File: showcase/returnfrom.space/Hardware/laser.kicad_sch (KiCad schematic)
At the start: 12 parts, among them J20 Conn_01x08_Socket, Q2 NPN, U7 LIS2DH

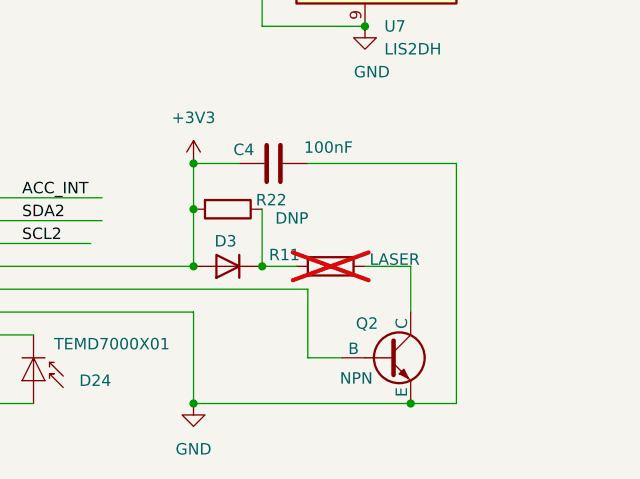
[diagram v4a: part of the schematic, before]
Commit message: Done. Ordered 50pcs. TO DO: clean-up, add BOM & POS
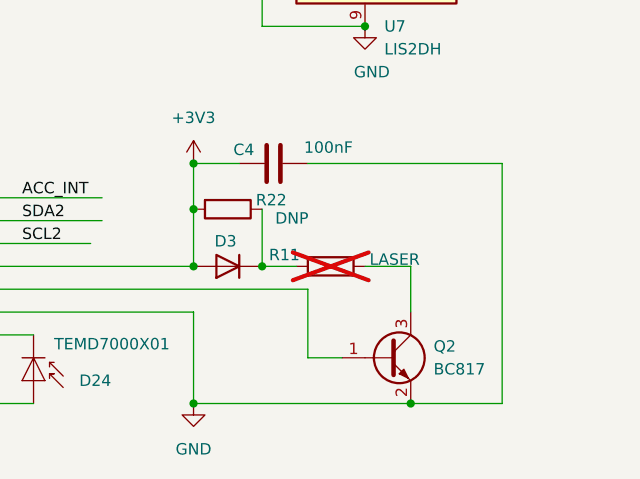
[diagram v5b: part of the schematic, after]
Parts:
- removed Q2: NPN, Package_TO_SOT_SMD:SOT-23, symbol Simulation_SPICE:NPN
- added Q2: BC817, Package_TO_SOT_SMD:SOT-23, symbol Transistor_BJT:BC817
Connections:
- net GND: now also Q2.2 (E)
- net at J20.4 (Pin_4): now also Q2.1 (B)
- net at R11.1: now also Q2.3 (C)
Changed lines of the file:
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@@
 	(paper "A4")
+	(junction
+		(at 204.47 120.65)
+		(diameter 0)
+		(color 0 0 0 0)
+	)
 	(junction
 		(at 180.34 99.06)
@@
 	)
 	(junction
-		(at 204.47 120.65)
-		(diameter 0)
-		(color 0 0 0 0)
-	)
-	(junction
 		(at 187.96 105.41)
 		(diameter 0)
@@
 	(wire
 		(pts
-			(xy 209.55 93.98) (xy 209.55 120.65)
+			(xy 214.63 93.98) (xy 214.63 120.65)
 		)
 		(stroke
@@
 	(wire
 		(pts
-			(xy 193.04 93.98) (xy 209.55 93.98)
+			(xy 193.04 93.98) (xy 214.63 93.98)
 		)
 		(stroke
@@
 	(wire
 		(pts
+			(xy 204.47 120.65) (xy 214.63 120.65)
+		)
+		(stroke
+			(width 0)
+			(type default)
+		)
+	)
+	(wire
+		(pts
 			(xy 158.75 97.79) (xy 170.18 97.79)
 		)
@@
 		(pts
 			(xy 201.93 50.8) (xy 212.09 50.8)
-		)
-		(stroke
-			(width 0)
-			(type default)
-		)
-	)
-	(wire
-		(pts
-			(xy 209.55 120.65) (xy 204.47 120.65)
 		)
 		(stroke
@@
 			)
 			(justify left bottom)
+		)
+	)
+	(symbol
+		(lib_id "Transistor_BJT:BC817")
+		(at 201.93 115.57 0)
+		(unit 1)
+		(exclude_from_sim no)
+		(in_bom yes)
+		(on_board yes)
+		(dnp no)
+		(fields_autoplaced yes)
+		(property "Reference" "Q2"
+			(at 207.01 114.2999 0)
+			(effects
+				(font
+					(size 1.27 1.27)
+				)
+				(justify left)
+			)
+		)
+		(property "Value" "BC817"
+			(at 207.01 116.8399 0)
+			(effects
+				(font
+					(size 1.27 1.27)
+				)
+				(justify left)
+			)
+		)
+		(property "Footprint" "Package_TO_SOT_SMD:SOT-23"
+			(at 207.01 117.475 0)
+			(effects
+				(font
+					(size 1.27 1.27)
+					(italic yes)
+				)
+				(justify left)
+				(hide yes)
+			)
+		)
+		(property "Datasheet" "https://www.onsemi.com/pub/Collateral/BC818-D.pdf"
+			(at 201.93 115.57 0)
+			(effects
+				(font
+					(size 1.27 1.27)
+				)
+				(justify left)
+				(hide yes)
+			)
+		)
+		(property "Description" "0.8A Ic, 45V Vce, NPN Transistor, SOT-23"
+			(at 201.93 115.57 0)
+			(effects
+				(font
+					(size 1.27 1.27)
+				)
+				(hide yes)
+			)
+		)
+		(pin "3"
+		)
+		(pin "2"
+		)
+		(pin "1"
+		)
+		(instances
+			(project ""
+				(path "/418a52ba-b136-48f0-a485-149e9dc1363e/b3f3025a-df4e-4d93-b3e9-df7af7ca410f"
+					(reference "Q2")
+					(unit 1)
+				)
+			)
 		)
 	)
@@
 					(unit 1)
 				)
-			)
-		)
-	)
-	(symbol
-		(lib_id "Simulation_SPICE:NPN")
-		(at 201.93 115.57 0)
-		(unit 1)
-		(exclude_from_sim no)
-		(in_bom yes)
-		(on_board yes)
-		(dnp no)
-		(property "Reference" "Q2"
-			(at 198.374 111.76 0)
-			(effects
-				(font
-					(size 1.27 1.27)
-				)
-				(justify left)
-			)
-		)
-		(property "Value" "NPN"
-			(at 196.596 117.856 0)
-			(effects
-				(font
-					(size 1.27 1.27)
-				)
-				(justify left)
-			)
-		)
-		(property "Footprint" "Package_TO_SOT_SMD:SOT-23"
-			(at 265.43 115.57 0)
-			(effects
-				(font
-					(size 1.27 1.27)
-				)
-				(hide yes)
-			)
-		)
-		(property "Datasheet" "https://ngspice.sourceforge.io/docs/ngspice-html-manual/manual.xhtml#cha_BJTs"
-			(at 265.43 115.57 0)
-			(effects
-				(font
-					(size 1.27 1.27)
-				)
-				(hide yes)
-			)
-		)
-		(property "Description" "Bipolar transistor symbol for simulation only, substrate tied to the emitter"
-			(at 201.93 115.57 0)
-			(effects
-				(font
-					(size 1.27 1.27)
-				)
-				(hide yes)
-			)
-		)
-		(property "Sim.Device" "NPN"
-			(at 201.93 115.57 0)
-			(effects
-				(font
-					(size 1.27 1.27)
-				)
-				(hide yes)
-			)
-		)
-		(property "Sim.Type" "GUMMELPOON"
-			(at 201.93 115.57 0)
-			(effects
-				(font
-					(size 1.27 1.27)
-				)
-				(hide yes)
-			)
-		)
-		(property "Sim.Pins" "1=C 2=B 3=E"
-			(at 201.93 115.57 0)
-			(effects
-				(font
-					(size 1.27 1.27)
-				)
-				(hide yes)
-			)
-		)
-		(pin "2"
-		)
-		(pin "1"
-		)
-		(pin "3"
-		)
-		(instances
-			(project ""
-				(path "/418a52ba-b136-48f0-a485-149e9dc1363e/b3f3025a-df4e-4d93-b3e9-df7af7ca410f"
-					(reference "Q2")
-					(unit 1)
-				)
